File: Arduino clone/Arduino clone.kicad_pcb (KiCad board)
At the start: 2 copper layers, 17 parts, among them J1 USART, J2 Digital pins, J3 ICSP, J4 I2C, U1 DS1337S+, U2 24LC1025, U3 24LC1025, U4 ATMEGA328P-AU, Y1 32MHz, Y2 16MHz

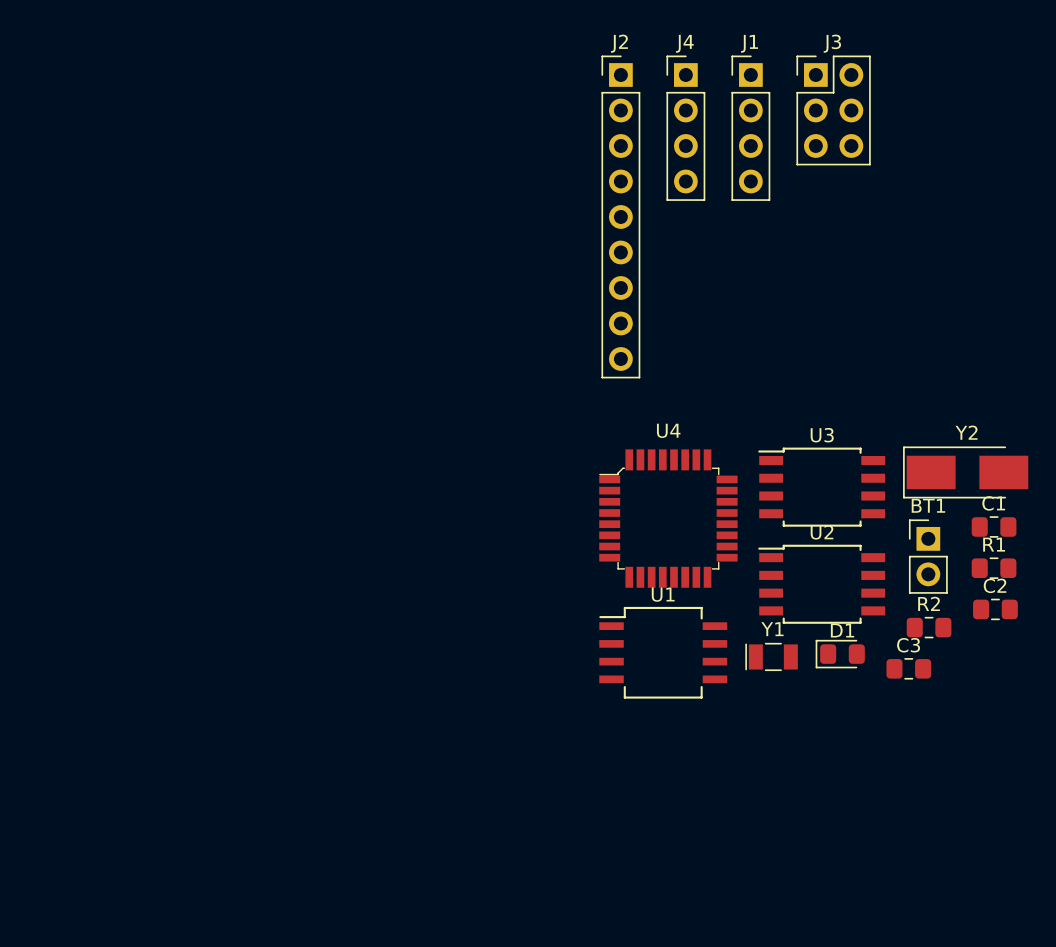
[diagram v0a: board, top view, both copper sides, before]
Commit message: Placing
Finished placing of components.
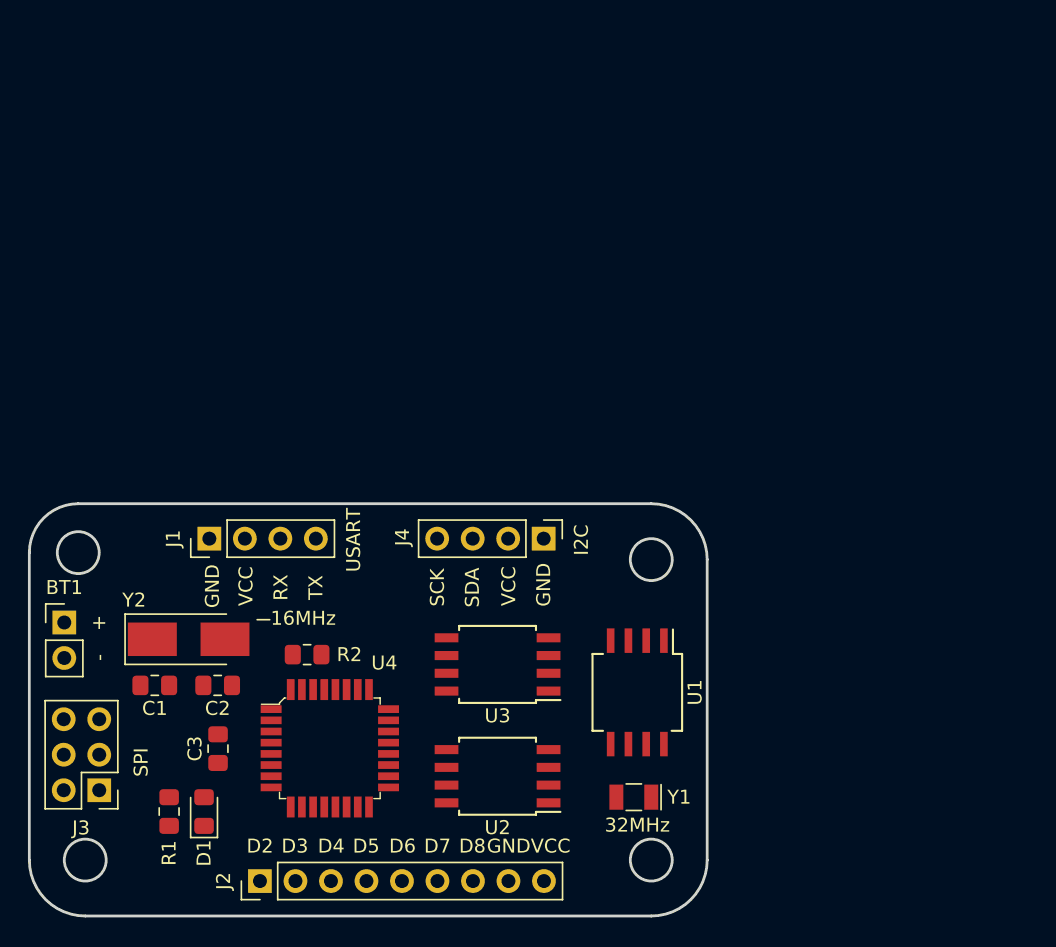
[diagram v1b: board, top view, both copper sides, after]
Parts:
- moved J3 72.4 mm to (101.0, 118.5), turned to 180 degrees
- moved J2 63.2 mm to (112.5, 125.0), turned to 90 degrees
- moved BT1 62.1 mm to (98.5, 106.5)
- moved R1 61.5 mm to (106.0, 120.0), turned to 90 degrees
- moved C1 61.1 mm to (105.0, 111.0), turned to 180 degrees
- moved Y2 57.0 mm to (107.4, 107.7)
- moved C2 55.9 mm to (109.5, 111.0), turned to 180 degrees
- moved J1 51.0 mm to (108.9, 100.5), turned to 90 degrees
- moved C3 49.8 mm to (109.5, 115.5), turned to 90 degrees
- moved D1 47.0 mm to (108.5, 120.0), turned to 90 degrees
- moved R2 44.5 mm to (115.9, 108.8), turned to 180 degrees
- moved J4 34.7 mm to (132.8, 100.5), turned to 270 degrees
- moved U4 29.3 mm to (117.5, 115.5)
- moved U2 27.0 mm to (129.5, 117.5), turned to 180 degrees
- moved U3 26.5 mm to (129.5, 109.5), turned to 180 degrees
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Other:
- board outline added: 48.5 x 29.5 mm
- board text added: "+"
- board text added: "-"
- board text added: "16MHz"
- board text added: "32MHz"
- board text added: "D2"
- board text added: "D3"
- board text added: "D4"
- board text added: "D5"
- board text added: "D6"
- board text added: "D7"
- board text added: "D8"
- board text added: "GND"
- board text added: "I2C"
- board text added: "RX"
- board text added: "SCK"
- board text added: "SDA"
- board text added: "SPI"
- board text added: "TX"
- board text added: "USART"
- board text added: "VCC"

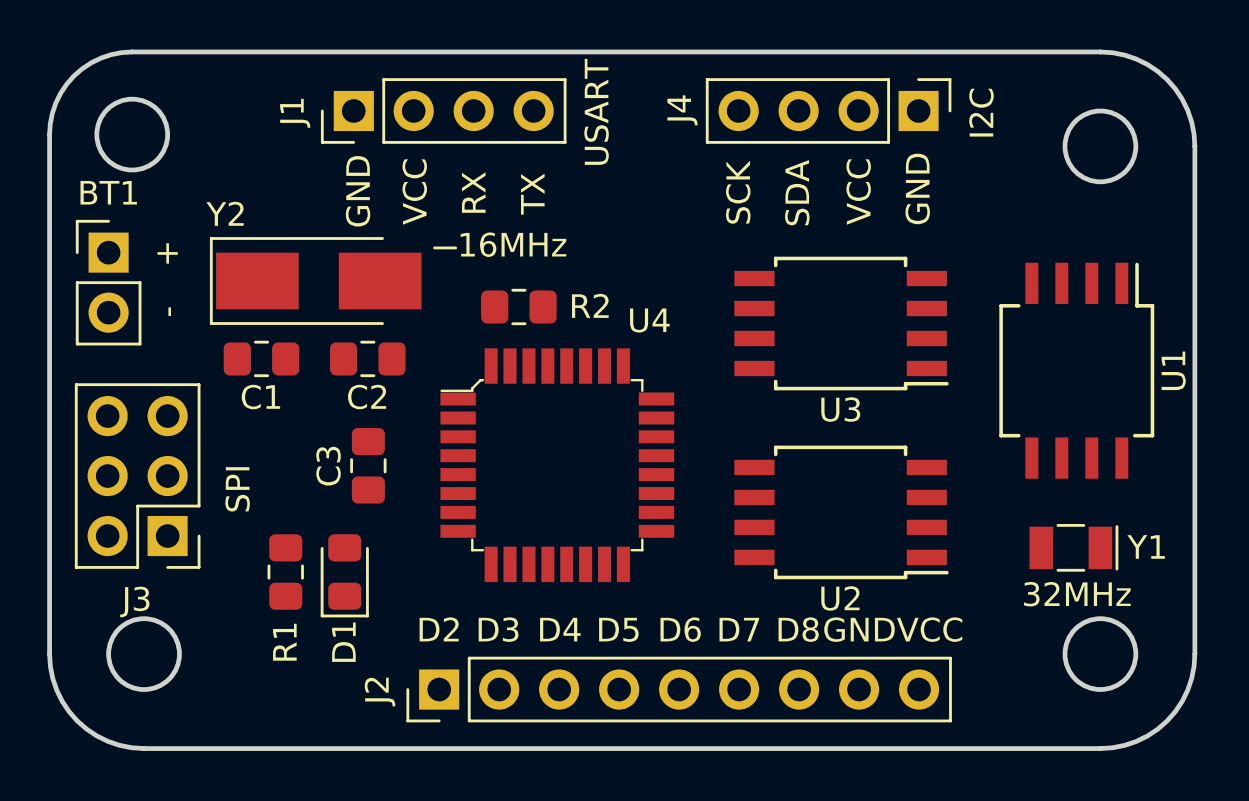
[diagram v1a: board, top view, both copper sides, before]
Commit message: Routing.
FInished routing.
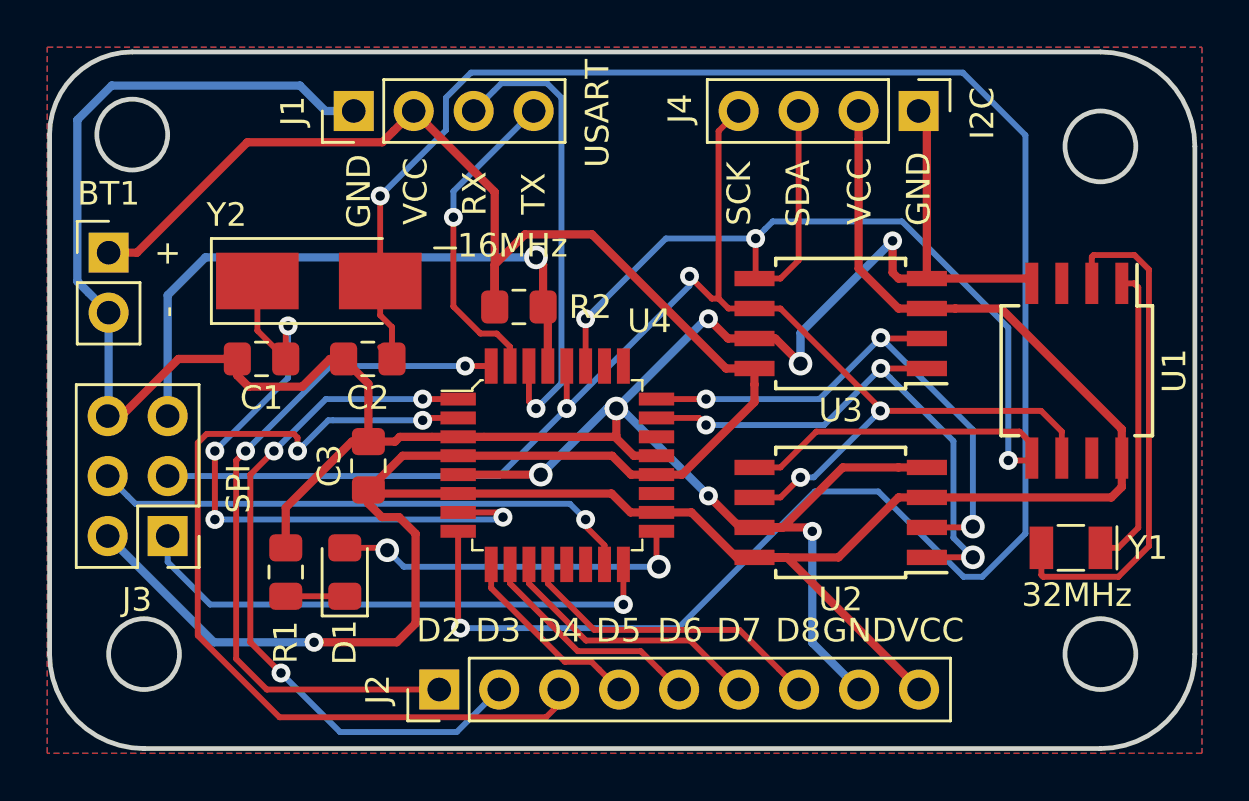
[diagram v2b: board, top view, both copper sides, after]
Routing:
- net /Vcc: track 0.00 -> 149.6 mm, vias 0 -> 1
- net GNDPWR: track 0.00 -> 128.2 mm, vias 0 -> 7
- net Net-(C2-Pad1): track 0.00 -> 88.8 mm, vias 0 -> 2
- net /SCK: track 0.00 -> 62.5 mm, vias 0 -> 4
- net /SDA: track 0.00 -> 53.6 mm, vias 0 -> 3
- net /D4: track 0.00 -> 38.1 mm, vias 0 -> 2
- net /D3: track 0.00 -> 30.1 mm, vias 0 -> 3
- net /D2: track 0.00 -> 30.0 mm, vias 0 -> 2
- net Net-(C1-Pad1): track 0.00 -> 28.9 mm, vias 0 -> 4
- net /RESET: track 0.00 -> 26.2 mm, vias 0 -> 1
- net /ADDS1: track 0.00 -> 24.1 mm, vias 0 -> 3
- net /ADDS2: track 0.00 -> 24.1 mm, vias 0 -> 3
- net /MOSI: track 0.00 -> 23.2 mm, vias 0 -> 1
- net /MISO: track 0.00 -> 22.8 mm, vias 0 -> 1
- net Net-(U1-Pad2): track 0.00 -> 21.8 mm
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- added copper zone on B.Cu, net GNDPWR
- added copper zone on F.Cu, net GNDPWR
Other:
- rule pad_to_mask_clearance: 0.061 -> 0.051
